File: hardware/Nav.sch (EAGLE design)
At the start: 52 parts

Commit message: Add nav board
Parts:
- removed BMP280: BMP280, bosch-bmp280:BMP280
- removed CA, CB: (no value), jst-ph:S2B-PH-K-S
- removed R1, R10, R20, R21, R22, R23, R24, R4, R8: 1k, resistor:R-US_R0603
- removed R11, R16, R17, R18, R19, R2, R3, R5, R6, R7, R9: 10k, resistor:R-US_R0603
- removed R12, R13, R14, R15: 100k, resistor:R-US_R0603
- removed SA, SB: (no value), jst-ph:S3B-PH-K-S
- removed STM32F072: STM32F072-LQFP48, stm32f0:STM32F072-LQFP48
- removed T1, T2, T3, T4: (no value), transistor-neu-to92:BC817-NPN-SOT23-BEC
- added D1, D2: RB521S-30TE61, RB521S-30TE61:RB521S-30TE61
- added I2C, UART: (no value), jst-ph:S4B-PH-K-S
- added IC1: BME280, bosch-bme280:BME280
- added U$1: STM32G431-LQFP48, stm32g4:STM32G431-LQFP48
- added U$3: DCK-3R3E, capacitors:DCK-3R3E
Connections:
- removed net !HIL!: GYSFFMANC.!RESET!, U$2.P1
- removed net CA: CA.2, R7.2, T3.C, U$2.P4
- removed net CAI: R7.1, R9.2, STM32F072.PA10/USART1_RX/TIM1_CH3
- removed net CAO: R8.1, STM32F072.PA11/USB_DM/CAN_RX
- removed net CB: CB.2, R11.2, STM32F072.PA8/TIM1_CH1, T4.C, U$2.P5
- removed net CBO: R10.1, STM32F072.PA9/USART1_TX/TIM1_CH2
- removed net N$10: R15.1, STM32F072.PA7/ADC_IN7/SPI1_MOSI/TIM3_CH2
- removed net N$11: R20.1, STM32F072.PA2/ADC_IN2/WKUP4USART2_TX
- removed net N$12: GYSFFMANC.UART_TXD, R21.2
- removed net N$13: R8.2, T3.B
- removed net N$14: R10.2, T4.B
- removed net N$15: R24.2, U$2.P8
- removed net N$16: R23.2, U$2.P7
- removed net N$17: R22.2, U$2.P6
- removed net N$34: R19.2, U$2.P12
- removed net N$35: R18.2, U$2.P11
- removed net N$36: R17.2, U$2.P10
- removed net N$43: R16.2, U$2.P9
- removed net N$5: R1.2, T1.B
- removed net N$6: R4.2, T2.B
- removed net N$7: R13.1, STM32F072.PA5/ADC_IN5/DAC_OUT2/SPI1_SCK
- removed net N$8: R14.1, STM32F072.PA6/ADC_IN6/SPI1_MISO/TIM3_CH1
- removed net SA: R2.2, SA.3, T1.E, U$2.P2
- removed net SAI: R2.1, R3.2, STM32F072.PB6USART1_TX/I2C1_SCL
- removed net SAO: R1.1, STM32F072.PB5/WKUP6/SPI1_MOSI/TIM3_CH2
- removed net SB: R5.2, SB.3, T2.E, U$2.P3
- removed net SBI: R5.1, R6.2, STM32F072.PB4/SPI1_MISO/TIM3_CH1
- removed net SBO: R4.1, STM32F072.PB3/SPI1_SCK/TIM2_CH2
- new net N$3: GYSFFMANC.!RESET!, U$1.PB1
- new net SCL: I2C.4, U$1.PA9
- new net SDA: I2C.3, U$1.PA8
- new net VBACKUP: D1.K, D2.K, GYSFFMANC.VDD3V3_BACKUP, U$3.+
- net !CS_ACCEL!: now also U$1.PA4; no longer R12.2, R19.1
- net !CS_GYRO!: now also U$1.PA6; no longer R14.2, R17.1
- net !CS_MAG!: now also U$1.PA5; no longer R13.2, R18.1
- net !CS_PRESS!: now also IC1.CSB, U$1.PA7; no longer BMP280.CSB, R15.2, R16.1
- net CAN_RX: now also U$1.PA11; no longer STM32F072.PB8/I2C1_SCL/TIM16_CH1/CAN_RX
- net CAN_TX: now also U$1.PA12; no longer STM32F072.PB9/I2C1_SDA/TIM17_CH1/CAN_TX
- net DRDYM: now also U$1.PA0; no longer STM32F072.PA0/USART4_TX/WKUP1/ADC_IN0
- net GND: now also I2C.2, IC1.GND, U$1.VSS1, U$1.VSS2, U$1.VSS3, U$1.VSSA, U$3.-, UART.2; no longer BMP280.GND, R11.1, R3.1, R6.1, R9.1, SA.1, SB.1, STM32F072.VSSA(P8), STM32F072.VSS_1(P23), STM32F072.VSS_2(P35), STM32F072.VSS_3(P47), T3.E, T4.E
- net GPS_RX: now also GYSFFMANC.UART_TXD, U$1.PA3, UART.4; no longer R21.1, STM32F072.PA3/ADC_IN3/COMP2_INP/USART2_RX, U$2.P14
- net GPS_TX: now also U$1.PA2, UART.3; no longer R20.2, U$2.P13
- net MISO: now also IC1.SDO, U$1.PB14; no longer BMP280.SDO, R23.1, STM32F072.PB14/SPI2_MISO/I2C2_SDA
- net MOSI: now also IC1.SDI, U$1.PB15; no longer BMP280.SDI, R22.1, STM32F072.PB15/WKUP7/RTC_REFIN/SPI2_MOSI
- net N$2: now also GYSFFMANC.GIO_7(1PPS), U$1.PB0; no longer R12.1, STM32F072.PA4/ADC_IN4/DAC_OUT1
- net N$51: now also U$1.PA1; no longer STM32F072.PA1/ADC_IN1/COMP1_INP/USART4_RX
- net N$70: now also U$1.PC15-OSC32_OUT; no longer STM32F072.PC15/OSC32_OUT
- net N$71: now also U$1.PC14-OSC32_IN; no longer STM32F072.PC14/OSC32_IN
- net NRST1: no longer STM32F072.NRST(P7)
- net SCK: now also IC1.SCK, U$1.PB13; no longer BMP280.SCK, R24.1, STM32F072.PB13/SPI2_SCK/I2C2_SCL
- net SWCLK1: now also U$1.PA14; no longer STM32F072.PA14/USART2_TX/SWCLK
- net SWDIO1: now also U$1.PA13; no longer STM32F072.PA13/SWDIO
- net VBAT: now also D2.A, U$1.VBAT; no longer GYSFFMANC.VDD3V3_BACKUP, STM32F072.VBATT(P1)
- net VCC: no longer CA.1, SA.2, SB.2, T1.C, T2.C
- net VDD: now also D1.A, I2C.1, IC1.VDD, IC1.VDDIO, U$1.VDD1, U$1.VDD2, U$1.VDD3, U$1.VDDA, U$1.VREF+, UART.1; no longer BMP280.VDD, BMP280.VDDIO, CB.1, STM32F072.VDDA(P9), STM32F072.VDDIO2(P36), STM32F072.VDD_1(P24), STM32F072.VDD_2(P48)
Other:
- moved on the sheet: C10, C11, C12, C7, CL3, CL4, CRYSTAL

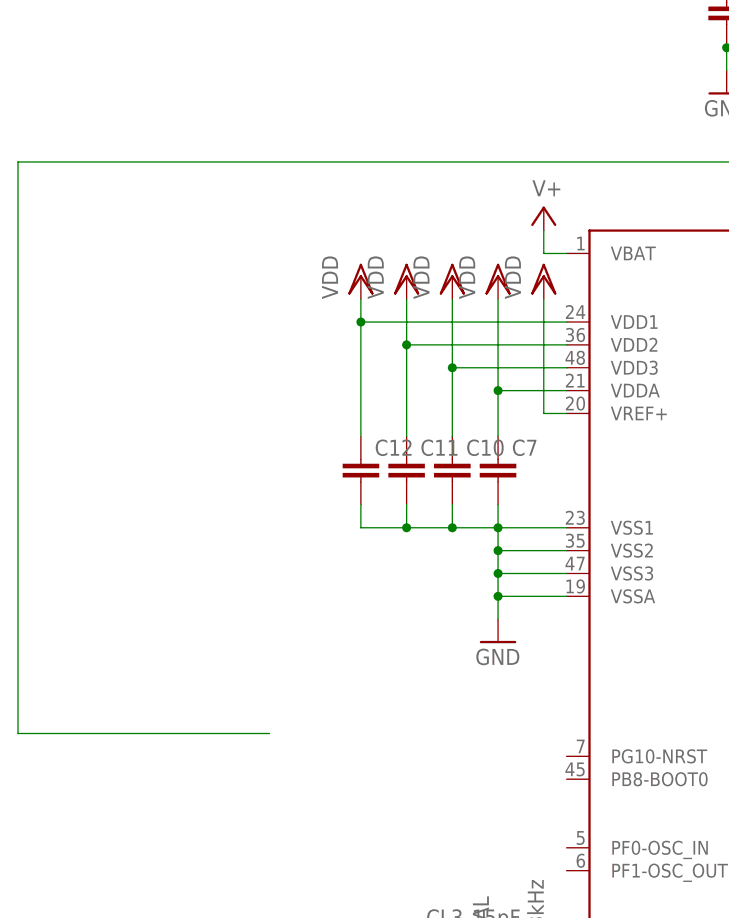
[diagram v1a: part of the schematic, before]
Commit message: Fix reset wire
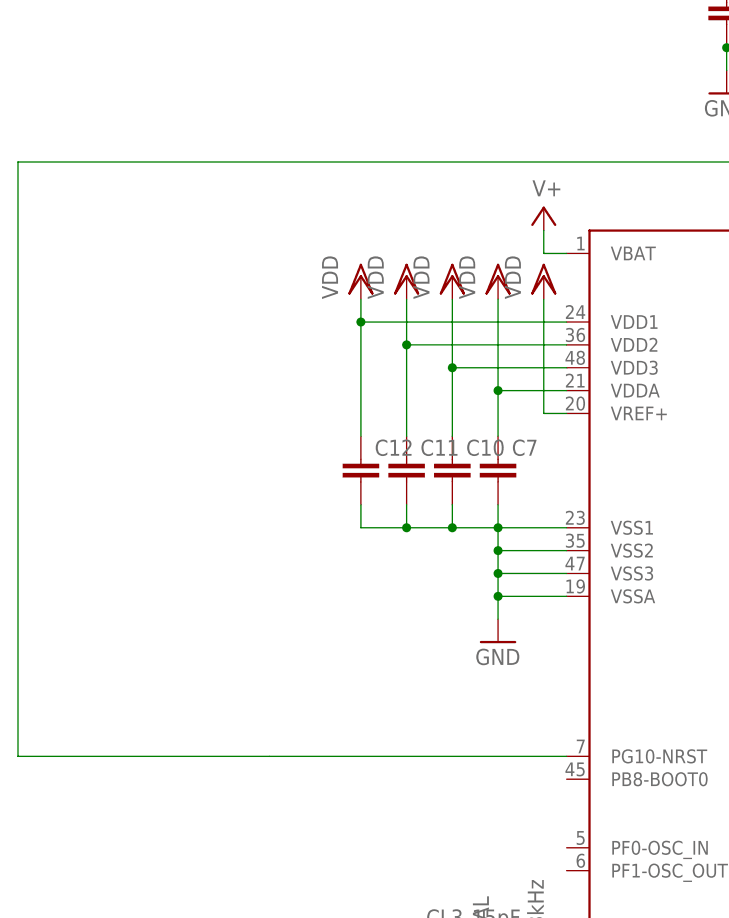
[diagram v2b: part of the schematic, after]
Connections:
- removed net NRST1: U$2.!RESET!
- new net N$4: U$1.PG10-NRST, U$2.!RESET!
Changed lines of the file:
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@@
-</segment>
-</net>
-<net name="NRST1" class="0">
-<segment>
-<wire x1="0" y1="43.18" x2="-27.94" y2="43.18" width="0.1524" layer="91"/>
-<wire x1="-27.94" y1="43.18" x2="-27.94" y2="106.68" width="0.1524" layer="91"/>
-<pinref part="U$2" gate="G$1" pin="!RESET!"/>
-<wire x1="-27.94" y1="106.68" x2="111.76" y2="106.68" width="0.1524" layer="91"/>
-<wire x1="111.76" y1="106.68" x2="111.76" y2="152.4" width="0.1524" layer="91"/>
 </segment>
 </net>
@@
 </segment>
 </net>
+<net name="N$4" class="0">
+<segment>
+<pinref part="U$1" gate="G$1" pin="PG10-NRST"/>
+<wire x1="33.02" y1="40.64" x2="0" y2="40.64" width="0.1524" layer="91"/>
+<wire x1="0" y1="40.64" x2="-27.94" y2="40.64" width="0.1524" layer="91"/>
+<wire x1="-27.94" y1="40.64" x2="-27.94" y2="106.68" width="0.1524" layer="91"/>
+<pinref part="U$2" gate="G$1" pin="!RESET!"/>
+<wire x1="-27.94" y1="106.68" x2="111.76" y2="106.68" width="0.1524" layer="91"/>
+<wire x1="111.76" y1="106.68" x2="111.76" y2="152.4" width="0.1524" layer="91"/>
+</segment>
+</net>
